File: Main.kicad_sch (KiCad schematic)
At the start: 2 parts, among them J5 OUT, J7 AC_IN

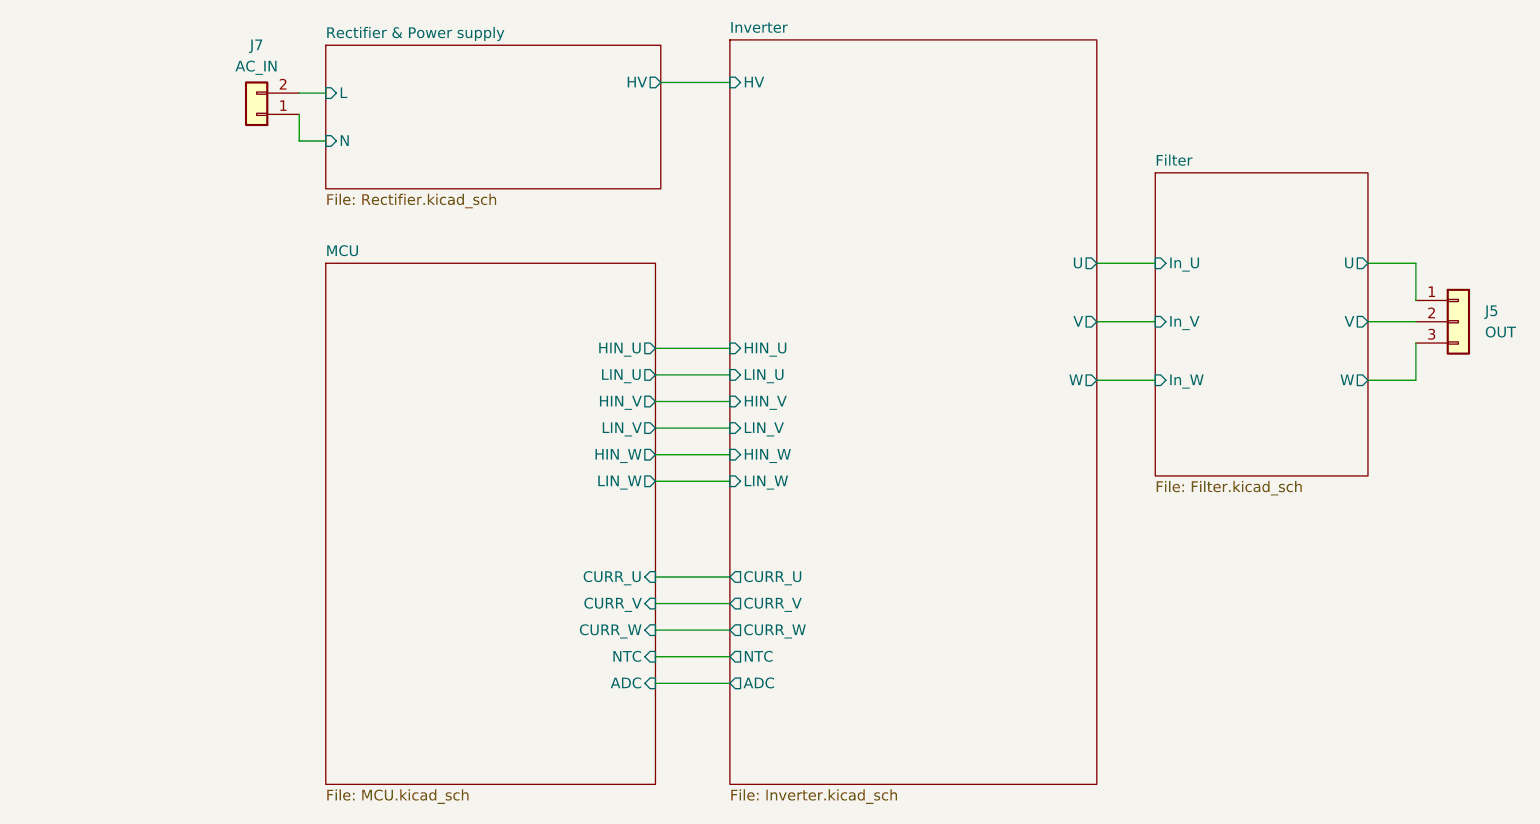
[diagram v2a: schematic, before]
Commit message: adding high speed isolator
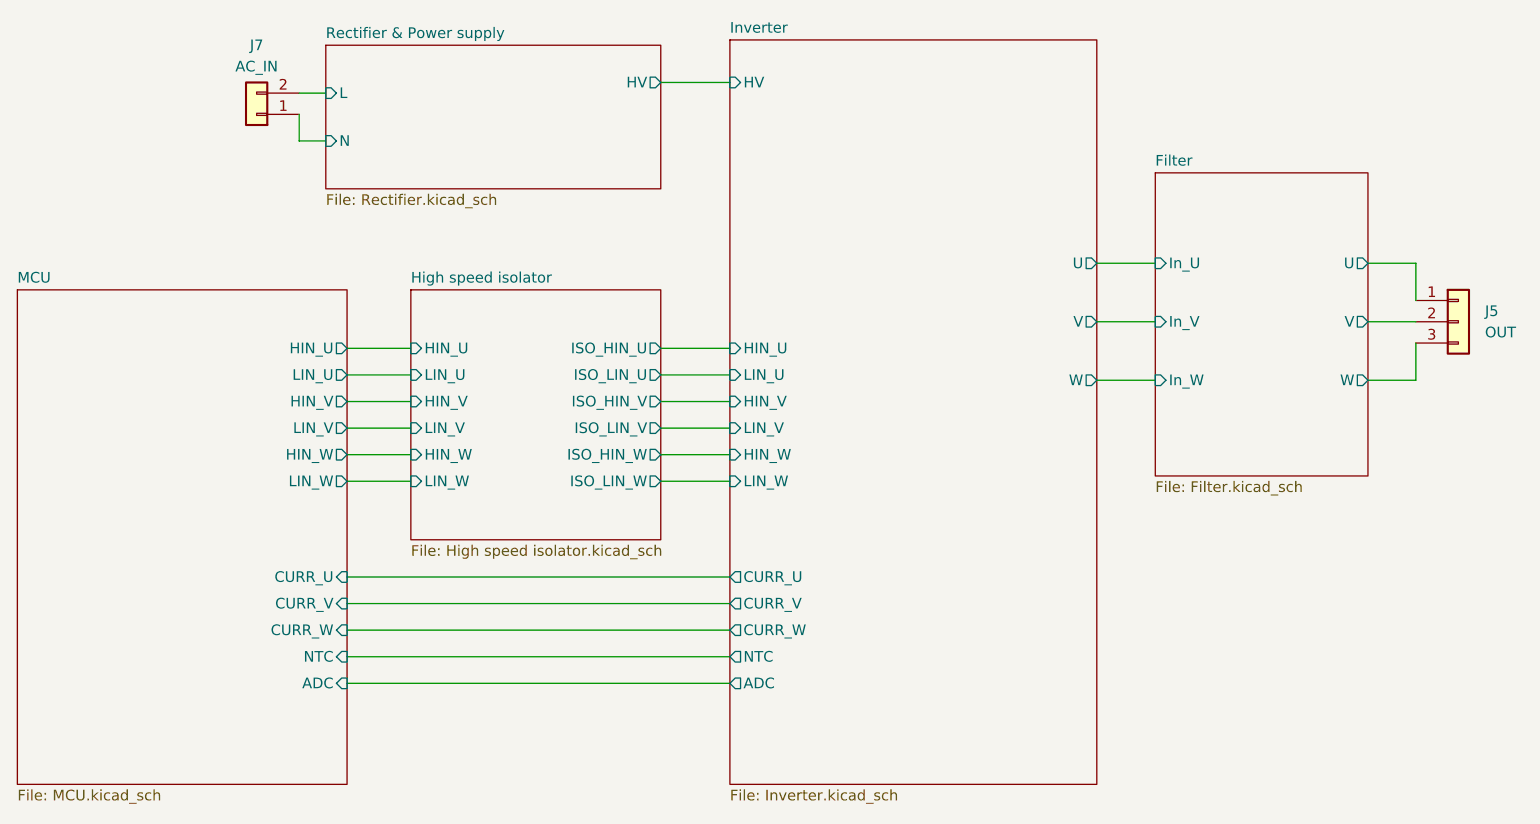
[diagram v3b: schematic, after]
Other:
- added sheet High speed isolator (High speed isolator.kicad_sch)
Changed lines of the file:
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@@
 (kicad_sch (version 20230121) (generator eeschema)
   (paper "A4")
+  (wire (pts (xy 88.9 85.09) (xy 96.52 85.09))
+    (stroke (width 0) (type default))
+  )
   (wire (pts (xy 210.82 85.725) (xy 216.535 85.725))
     (stroke (width 0) (type default))
   )
-  (wire (pts (xy 125.73 85.09) (xy 134.62 85.09))
-    (stroke (width 0) (type default))
-  )
-  (wire (pts (xy 125.73 118.745) (xy 134.62 118.745))
-    (stroke (width 0) (type default))
-  )
-  (wire (pts (xy 125.73 88.265) (xy 134.62 88.265))
-    (stroke (width 0) (type default))
-  )
-  (wire (pts (xy 125.73 94.615) (xy 134.62 94.615))
+  (wire (pts (xy 88.9 118.745) (xy 134.62 118.745))
+    (stroke (width 0) (type default))
+  )
+  (wire (pts (xy 88.9 88.265) (xy 96.52 88.265))
     (stroke (width 0) (type default))
   )
@@
     (stroke (width 0) (type default))
   )
-  (wire (pts (xy 125.73 112.395) (xy 134.62 112.395))
+  (wire (pts (xy 88.9 112.395) (xy 134.62 112.395))
     (stroke (width 0) (type default))
   )
@@
     (stroke (width 0) (type default))
   )
+  (wire (pts (xy 126.365 88.265) (xy 134.62 88.265))
+    (stroke (width 0) (type default))
+  )
   (wire (pts (xy 210.82 71.755) (xy 216.535 71.755))
     (stroke (width 0) (type default))
@@
     (stroke (width 0) (type default))
   )
-  (wire (pts (xy 125.73 115.57) (xy 134.62 115.57))
+  (wire (pts (xy 88.9 91.44) (xy 96.52 91.44))
+    (stroke (width 0) (type default))
+  )
+  (wire (pts (xy 88.9 97.79) (xy 96.52 97.79))
+    (stroke (width 0) (type default))
+  )
+  (wire (pts (xy 88.9 115.57) (xy 134.62 115.57))
     (stroke (width 0) (type default))
   )
@@
     (stroke (width 0) (type default))
   )
-  (wire (pts (xy 125.73 91.44) (xy 134.62 91.44))
-    (stroke (width 0) (type default))
-  )
-  (wire (pts (xy 125.73 109.22) (xy 134.62 109.22))
+  (wire (pts (xy 126.365 97.79) (xy 134.62 97.79))
+    (stroke (width 0) (type default))
+  )
+  (wire (pts (xy 88.9 109.22) (xy 134.62 109.22))
     (stroke (width 0) (type default))
   )
@@
     (stroke (width 0) (type default))
   )
-  (wire (pts (xy 125.73 121.92) (xy 134.62 121.92))
+  (wire (pts (xy 88.9 121.92) (xy 134.62 121.92))
+    (stroke (width 0) (type default))
+  )
+  (wire (pts (xy 88.9 94.615) (xy 96.52 94.615))
     (stroke (width 0) (type default))
   )
@@
     (stroke (width 0) (type default))
   )
+  (wire (pts (xy 126.365 81.915) (xy 134.62 81.915))
+    (stroke (width 0) (type default))
+  )
   (wire (pts (xy 216.535 71.755) (xy 216.535 76.2))
     (stroke (width 0) (type default))
   )
-  (wire (pts (xy 125.73 97.79) (xy 134.62 97.79))
-    (stroke (width 0) (type default))
-  )
-  (wire (pts (xy 125.73 81.915) (xy 134.62 81.915))
+  (wire (pts (xy 88.9 81.915) (xy 96.52 81.915))
+    (stroke (width 0) (type default))
+  )
+  (wire (pts (xy 126.365 85.09) (xy 134.62 85.09))
+    (stroke (width 0) (type default))
+  )
+  (wire (pts (xy 126.365 94.615) (xy 134.62 94.615))
+    (stroke (width 0) (type default))
+  )
+  (wire (pts (xy 126.365 91.44) (xy 134.62 91.44))
     (stroke (width 0) (type default))
   )
@@
     )
   )
-  (sheet (at 86.36 71.755) (size 39.37 62.23) (fields_autoplaced)
+  (sheet (at 96.52 74.93) (size 29.845 29.845) (fields_autoplaced)
     (stroke (width 0.1524) (type solid))
     (fill (color 0 0 0 0.0000))
-    (property "Sheetname" "MCU" (at 86.36 71.0434 0)
+    (property "Sheetname" "High speed isolator" (at 96.52 74.2184 0)
       (effects (font (size 1.27 1.27)) (justify left bottom))
     )
-    (property "Sheetfile" "MCU.kicad_sch" (at 86.36 134.5696 0)
+    (property "Sheetfile" "High speed isolator.kicad_sch" (at 96.52 105.3596 0)
       (effects (font (size 1.27 1.27)) (justify left top))
     )
-    (pin "HIN_U" output (at 125.73 81.915 0)
-      (effects (font (size 1.27 1.27)) (justify right))
-    )
-    (pin "HIN_V" output (at 125.73 88.265 0)
-      (effects (font (size 1.27 1.27)) (justify right))
-    )
-    (pin "LIN_V" output (at 125.73 91.44 0)
-      (effects (font (size 1.27 1.27)) (justify right))
-    )
-    (pin "LIN_U" output (at 125.73 85.09 0)
-      (effects (font (size 1.27 1.27)) (justify right))
-    )
-    (pin "HIN_W" output (at 125.73 94.615 0)
-      (effects (font (size 1.27 1.27)) (justify right))
-    )
-    (pin "LIN_W" output (at 125.73 97.79 0)
-      (effects (font (size 1.27 1.27)) (justify right))
-    )
-    (pin "CURR_V" input (at 125.73 112.395 0)
-      (effects (font (size 1.27 1.27)) (justify right))
-    )
-    (pin "CURR_U" input (at 125.73 109.22 0)
-      (effects (font (size 1.27 1.27)) (justify right))
-    )
-    (pin "NTC" input (at 125.73 118.745 0)
-      (effects (font (size 1.27 1.27)) (justify right))
-    )
-    (pin "CURR_W" input (at 125.73 115.57 0)
-      (effects (font (size 1.27 1.27)) (justify right))
-    )
-    (pin "ADC" input (at 125.73 121.92 0)
-      (effects (font (size 1.27 1.27)) (justify right))
-    )
+    (pin "HIN_W" input (at 96.52 94.615 180)
+      (effects (font (size 1.27 1.27)) (justify left))
+    )
+    (pin "LIN_U" input (at 96.52 85.09 180)
+      (effects (font (size 1.27 1.27)) (justify left))
+    )
+    (pin "HIN_V" input (at 96.52 88.265 180)
+      (effects (font (size 1.27 1.27)) (justify left))
+    )
+    (pin "HIN_U" input (at 96.52 81.915 180)
+      (effects (font (size 1.27 1.27)) (justify left))
+    )
+    (pin "LIN_W" input (at 96.52 97.79 180)
+      (effects (font (size 1.27 1.27)) (justify left))
+    )
+    (pin "LIN_V" input (at 96.52 91.44 180)
+      (effects (font (size 1.27 1.27)) (justify left))
+    )
+    (pin "ISO_LIN_W" output (at 126.365 97.79 0)
+      (effects (font (size 1.27 1.27)) (justify right))
+    )
+    (pin "ISO_LIN_U" output (at 126.365 85.09 0)
+      (effects (font (size 1.27 1.27)) (justify right))
+    )
+    (pin "ISO_HIN_V" output (at 126.365 88.265 0)
+      (effects (font (size 1.27 1.27)) (justify right))
+    )
+    (pin "ISO_LIN_V" output (at 126.365 91.44 0)
+      (effects (font (size 1.27 1.27)) (justify right))
+    )
+    (pin "ISO_HIN_W" output (at 126.365 94.615 0)
+      (effects (font (size 1.27 1.27)) (justify right))
+    )
+    (pin "ISO_HIN_U" output (at 126.365 81.915 0)
+      (effects (font (size 1.27 1.27)) (justify right))
+    )
+    (instances
+      (project "Main"
+        (path "/c97a22ab-71f8-4b91-b313-15b8a3e640d7" (page "6"))
+      )
+    )
+  )
+  (sheet (at 49.53 74.93) (size 39.37 59.055) (fields_autoplaced)
+    (stroke (width 0.1524) (type solid))
+    (fill (color 0 0 0 0.0000))
+    (property "Sheetname" "MCU" (at 49.53 74.2184 0)
+      (effects (font (size 1.27 1.27)) (justify left bottom))
+    )
+    (property "Sheetfile" "MCU.kicad_sch" (at 49.53 134.5696 0)
+      (effects (font (size 1.27 1.27)) (justify left top))
+    )
+    (pin "HIN_U" output (at 88.9 81.915 0)
+      (effects (font (size 1.27 1.27)) (justify right))
+    )
+    (pin "HIN_V" output (at 88.9 88.265 0)
+      (effects (font (size 1.27 1.27)) (justify right))
+    )
+    (pin "LIN_V" output (at 88.9 91.44 0)
+      (effects (font (size 1.27 1.27)) (justify right))
+    )
+    (pin "LIN_U" output (at 88.9 85.09 0)
+      (effects (font (size 1.27 1.27)) (justify right))
+    )
+    (pin "HIN_W" output (at 88.9 94.615 0)
+      (effects (font (size 1.27 1.27)) (justify right))
+    )
+    (pin "LIN_W" output (at 88.9 97.79 0)
+      (effects (font (size 1.27 1.27)) (justify right))
+    )
+    (pin "CURR_V" input (at 88.9 112.395 0)
+      (effects (font (size 1.27 1.27)) (justify right))
+    )
+    (pin "CURR_U" input (at 88.9 109.22 0)
+      (effects (font (size 1.27 1.27)) (justify right))
+    )
+    (pin "NTC" input (at 88.9 118.745 0)
+      (effects (font (size 1.27 1.27)) (justify right))
+    )
+    (pin "CURR_W" input (at 88.9 115.57 0)
+      (effects (font (size 1.27 1.27)) (justify right))
+    )
+    (pin "ADC" input (at 88.9 121.92 0)
+      (effects (font (size 1.27 1.27)) (justify right))
+    )

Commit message: update footprint
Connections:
- net Filter/U renamed Inverter/U
- net Filter/V renamed Inverter/V
- net Filter/W renamed Inverter/W
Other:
- removed sheet Filter
- removed sheet High speed isolator
- moved on the sheet: J5
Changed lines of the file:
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@@
 (kicad_sch (version 20230121) (generator eeschema)
   (paper "A4")
-  (wire (pts (xy 88.9 85.09) (xy 96.52 85.09))
+  (wire (pts (xy 126.365 118.745) (xy 134.62 118.745))
     (stroke (width 0) (type default))
   )
-  (wire (pts (xy 210.82 85.725) (xy 216.535 85.725))
-    (stroke (width 0) (type default))
-  )
-  (wire (pts (xy 88.9 118.745) (xy 134.62 118.745))
-    (stroke (width 0) (type default))
-  )
-  (wire (pts (xy 88.9 88.265) (xy 96.52 88.265))
+  (wire (pts (xy 185.42 81.28) (xy 185.42 85.725))
     (stroke (width 0) (type default))
   )
@@
     (stroke (width 0) (type default))
   )
-  (wire (pts (xy 88.9 112.395) (xy 134.62 112.395))
+  (wire (pts (xy 126.365 112.395) (xy 134.62 112.395))
     (stroke (width 0) (type default))
   )
@@
     (stroke (width 0) (type default))
   )
+  (wire (pts (xy 178.435 78.74) (xy 185.42 78.74))
+    (stroke (width 0) (type default))
+  )
+  (wire (pts (xy 126.365 81.915) (xy 134.62 81.915))
+    (stroke (width 0) (type default))
+  )
   (wire (pts (xy 126.365 88.265) (xy 134.62 88.265))
     (stroke (width 0) (type default))
   )
-  (wire (pts (xy 210.82 71.755) (xy 216.535 71.755))
+  (wire (pts (xy 126.365 115.57) (xy 134.62 115.57))
     (stroke (width 0) (type default))
   )
-  (wire (pts (xy 178.435 78.74) (xy 185.42 78.74))
-    (stroke (width 0) (type default))
-  )
-  (wire (pts (xy 88.9 91.44) (xy 96.52 91.44))
-    (stroke (width 0) (type default))
-  )
-  (wire (pts (xy 88.9 97.79) (xy 96.52 97.79))
-    (stroke (width 0) (type default))
-  )
-  (wire (pts (xy 88.9 115.57) (xy 134.62 115.57))
+  (wire (pts (xy 126.365 91.44) (xy 134.62 91.44))
     (stroke (width 0) (type default))
   )
@@
     (stroke (width 0) (type default))
   )
-  (wire (pts (xy 216.535 81.28) (xy 216.535 85.725))
+  (wire (pts (xy 126.365 94.615) (xy 134.62 94.615))
     (stroke (width 0) (type default))
   )
-  (wire (pts (xy 126.365 97.79) (xy 134.62 97.79))
-    (stroke (width 0) (type default))
-  )
-  (wire (pts (xy 88.9 109.22) (xy 134.62 109.22))
+  (wire (pts (xy 126.365 109.22) (xy 134.62 109.22))
     (stroke (width 0) (type default))
   )
@@
     (stroke (width 0) (type default))
   )
-  (wire (pts (xy 88.9 121.92) (xy 134.62 121.92))
+  (wire (pts (xy 126.365 121.92) (xy 134.62 121.92))
     (stroke (width 0) (type default))
   )
-  (wire (pts (xy 88.9 94.615) (xy 96.52 94.615))
+  (wire (pts (xy 126.365 97.79) (xy 134.62 97.79))
     (stroke (width 0) (type default))
   )
-  (wire (pts (xy 210.82 78.74) (xy 216.535 78.74))
-    (stroke (width 0) (type default))
-  )
-  (wire (pts (xy 126.365 81.915) (xy 134.62 81.915))
-    (stroke (width 0) (type default))
-  )
-  (wire (pts (xy 216.535 71.755) (xy 216.535 76.2))
-    (stroke (width 0) (type default))
-  )
-  (wire (pts (xy 88.9 81.915) (xy 96.52 81.915))
+  (wire (pts (xy 185.42 71.755) (xy 185.42 76.2))
     (stroke (width 0) (type default))
   )
@@
     (stroke (width 0) (type default))
   )
-  (wire (pts (xy 126.365 94.615) (xy 134.62 94.615))
-    (stroke (width 0) (type default))
-  )
-  (wire (pts (xy 126.365 91.44) (xy 134.62 91.44))
-    (stroke (width 0) (type default))
-  )
-  (symbol (lib_id "Connector_Generic:Conn_01x03") (at 221.615 78.74 0) (unit 1)
+  (symbol (lib_id "Connector_Generic:Conn_01x03") (at 190.5 78.74 0) (unit 1)
     (in_bom yes) (on_board yes) (dnp no) (fields_autoplaced)
-    (property "Reference" "J5" (at 224.79 77.47 0)
+    (property "Reference" "J5" (at 193.675 77.47 0)
       (effects (font (size 1.27 1.27)) (justify left))
     )
-    (property "Value" "OUT" (at 224.79 80.01 0)
+    (property "Value" "OUT" (at 193.675 80.01 0)
       (effects (font (size 1.27 1.27)) (justify left))
     )
-    (property "Footprint" "" (at 221.615 78.74 0)
+    (property "Footprint" "" (at 190.5 78.74 0)
       (effects (font (size 1.27 1.27)) hide)
     )
-    (property "Datasheet" "~" (at 221.615 78.74 0)
+    (property "Datasheet" "~" (at 190.5 78.74 0)
       (effects (font (size 1.27 1.27)) hide)
     )
@@
     )
   )
-  (sheet (at 96.52 74.93) (size 29.845 29.845) (fields_autoplaced)
+  (sheet (at 86.995 74.93) (size 39.37 59.055) (fields_autoplaced)
     (stroke (width 0.1524) (type solid))
     (fill (color 0 0 0 0.0000))
-    (property "Sheetname" "High speed isolator" (at 96.52 74.2184 0)
+    (property "Sheetname" "MCU" (at 86.995 74.2184 0)
       (effects (font (size 1.27 1.27)) (justify left bottom))
     )
-    (property "Sheetfile" "High speed isolator.kicad_sch" (at 96.52 105.3596 0)
+    (property "Sheetfile" "MCU.kicad_sch" (at 86.995 134.5696 0)
       (effects (font (size 1.27 1.27)) (justify left top))
     )
-    (pin "HIN_W" input (at 96.52 94.615 180)
-      (effects (font (size 1.27 1.27)) (justify left))
-    )
-    (pin "LIN_U" input (at 96.52 85.09 180)
-      (effects (font (size 1.27 1.27)) (justify left))
-    )
-    (pin "HIN_V" input (at 96.52 88.265 180)
-      (effects (font (size 1.27 1.27)) (justify left))
-    )
-    (pin "HIN_U" input (at 96.52 81.915 180)
-      (effects (font (size 1.27 1.27)) (justify left))
-    )
-    (pin "LIN_W" input (at 96.52 97.79 180)
-      (effects (font (size 1.27 1.27)) (justify left))
-    )
-    (pin "LIN_V" input (at 96.52 91.44 180)
-      (effects (font (size 1.27 1.27)) (justify left))
-    )
-    (pin "ISO_LIN_W" output (at 126.365 97.79 0)
+    (pin "HIN_U" output (at 126.365 81.915 0)
       (effects (font (size 1.27 1.27)) (justify right))
     )
-    (pin "ISO_LIN_U" output (at 126.365 85.09 0)
+    (pin "HIN_V" output (at 126.365 88.265 0)
       (effects (font (size 1.27 1.27)) (justify right))
     )
-    (pin "ISO_HIN_V" output (at 126.365 88.265 0)
+    (pin "LIN_V" output (at 126.365 91.44 0)
       (effects (font (size 1.27 1.27)) (justify right))
     )
-    (pin "ISO_LIN_V" output (at 126.365 91.44 0)
+    (pin "LIN_U" output (at 126.365 85.09 0)
       (effects (font (size 1.27 1.27)) (justify right))
     )
-    (pin "ISO_HIN_W" output (at 126.365 94.615 0)
+    (pin "HIN_W" output (at 126.365 94.615 0)
       (effects (font (size 1.27 1.27)) (justify right))
     )
-    (pin "ISO_HIN_U" output (at 126.365 81.915 0)
+    (pin "LIN_W" output (at 126.365 97.79 0)
       (effects (font (size 1.27 1.27)) (justify right))
     )
-    (instances
-      (project "Main"
-        (path "/c97a22ab-71f8-4b91-b313-15b8a3e640d7" (page "6"))
-      )
-    )
-  )
-  (sheet (at 49.53 74.93) (size 39.37 59.055) (fields_autoplaced)
-    (stroke (width 0.1524) (type solid))
-    (fill (color 0 0 0 0.0000))
-    (property "Sheetname" "MCU" (at 49.53 74.2184 0)
-      (effects (font (size 1.27 1.27)) (justify left bottom))
-    )
-    (property "Sheetfile" "MCU.kicad_sch" (at 49.53 134.5696 0)
-      (effects (font (size 1.27 1.27)) (justify left top))
-    )
-    (pin "HIN_U" output (at 88.9 81.915 0)
+    (pin "CURR_V" input (at 126.365 112.395 0)
       (effects (font (size 1.27 1.27)) (justify right))
     )
-    (pin "HIN_V" output (at 88.9 88.265 0)
+    (pin "CURR_U" input (at 126.365 109.22 0)
       (effects (font (size 1.27 1.27)) (justify right))
     )
-    (pin "LIN_V" output (at 88.9 91.44 0)
+    (pin "NTC" input (at 126.365 118.745 0)
       (effects (font (size 1.27 1.27)) (justify right))
     )
-    (pin "LIN_U" output (at 88.9 85.09 0)
+    (pin "CURR_W" input (at 126.365 115.57 0)
       (effects (font (size 1.27 1.27)) (justify right))
     )
-    (pin "HIN_W" output (at 88.9 94.615 0)
-      (effects (font (size 1.27 1.27)) (justify right))
-    )
-    (pin "LIN_W" output (at 88.9 97.79 0)
-      (effects (font (size 1.27 1.27)) (justify right))
-    )
-    (pin "CURR_V" input (at 88.9 112.395 0)
-      (effects (font (size 1.27 1.27)) (justify right))
-    )
-    (pin "CURR_U" input (at 88.9 109.22 0)
-      (effects (font (size 1.27 1.27)) (justify right))
-    )
-    (pin "NTC" input (at 88.9 118.745 0)
-      (effects (font (size 1.27 1.27)) (justify right))
-    )
-    (pin "CURR_W" input (at 88.9 115.57 0)
-      (effects (font (size 1.27 1.27)) (justify right))
-    )
-    (pin "ADC" input (at 88.9 121.92 0)
+    (pin "ADC" input (at 126.365 121.92 0)
       (effects (font (size 1.27 1.27)) (justify right))
     )
@@
       )
     )
-  )
-  (sheet (at 185.42 60.96) (size 25.4 36.195) (fields_autoplaced)
-    (stroke (width 0.1524) (type solid))
-    (fill (color 0 0 0 0.0000))
-    (property "Sheetname" "Filter" (at 185.42 60.2484 0)
-      (effects (font (size 1.27 1.27)) (justify left bottom))
-    )
-    (property "Sheetfile" "Filter.kicad_sch" (at 185.42 97.7396 0)
-      (effects (font (size 1.27 1.27)) (justify left top))
-    )
-    (pin "U" output (at 210.82 71.755 0)
-      (effects (font (size 1.27 1.27)) (justify right))
-    )
-    (pin "In_W" input (at 185.42 85.725 180)
-      (effects (font (size 1.27 1.27)) (justify left))
-    )
-    (pin "In_U" input (at 185.42 71.755 180)
-      (effects (font (size 1.27 1.27)) (justify left))
-    )
-    (pin "In_V" input (at 185.42 78.74 180)
-      (effects (font (size 1.27 1.27)) (justify left))
-    )
-    (pin "V" output (at 210.82 78.74 0)
-      (effects (font (size 1.27 1.27)) (justify right))
-    )
-    (pin "W" output (at 210.82 85.725 0)
-      (effects (font (size 1.27 1.27)) (justify right))
-    )
-    (instances
-      (project "Main"
-        (path "/c97a22ab-71f8-4b91-b313-15b8a3e640d7" (page "5"))
-      )
-    )
